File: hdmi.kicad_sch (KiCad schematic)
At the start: 58 parts, among them J13 HDMI-Mini-C_WE_685119136923, Q1 PJE138K, Q12 PJE138K, Q2 PJE138K, Q3 PJE138K, U36 TS3DV642RUARQ1, U43 NTS0102_XSON, U44 TPD4E05U06QDQARQ1, U45 TPD4E05U06QDQARQ1, U46 TPD4E05U06QDQARQ1

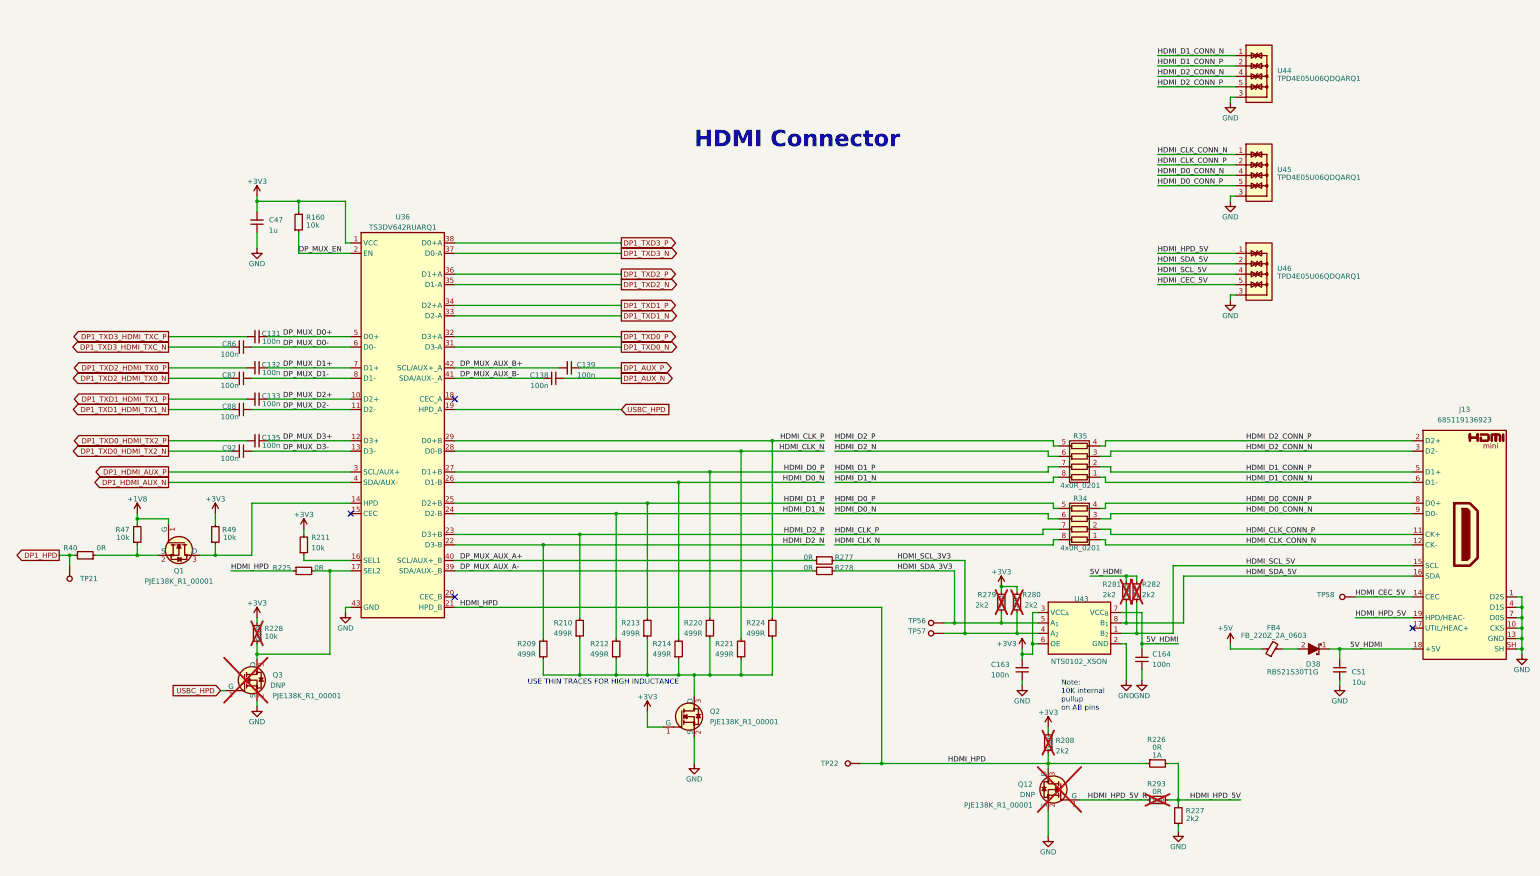
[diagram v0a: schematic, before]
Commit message: Schematic complete. Partial routing
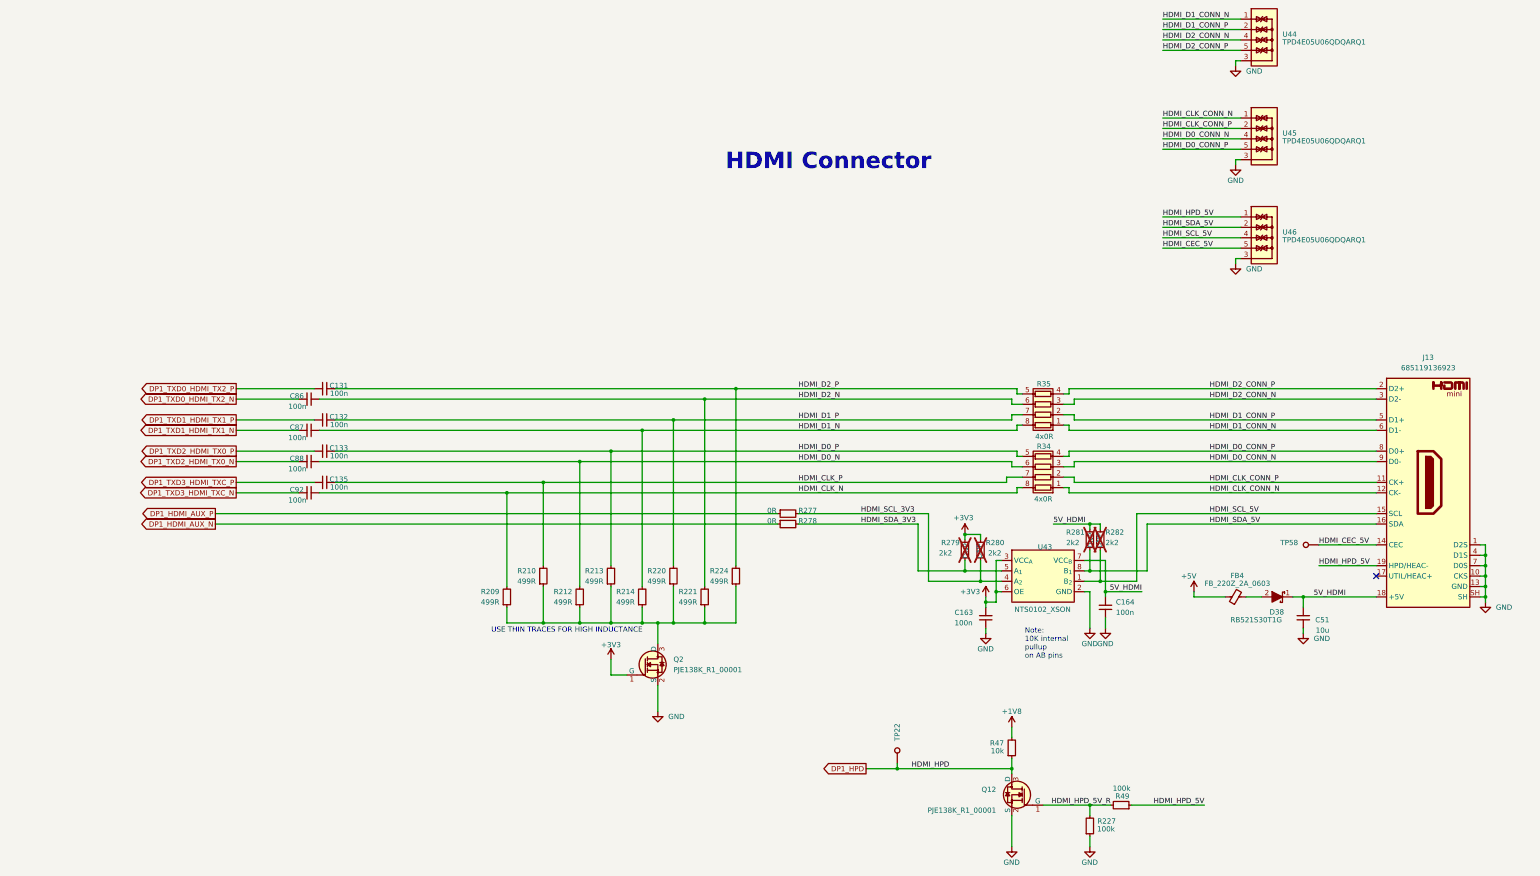
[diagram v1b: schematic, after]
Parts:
- removed C138, C139: C_100n_0402, antmicro-footprints:C_0402_1005Metric, symbol antmicroCapacitors0402:C_100n_0402
- removed C47: C_1u_0402, antmicro-footprints:C_0402_1005Metric, symbol antmicroCapacitors0402:C_1u_0402
- removed Q1, Q3: PJE138K, antmicro-footprints:SOT-523, symbol antmicroTransistorsFETsMOSFETsSingle:PJE138K
- removed R160, R211, R228, R49: R_10k_0402, antmicro-footprints:R_0402_1005Metric, symbol antmicroResistors0402:R_10k_0402
- removed R208: R_2k2_0402, antmicro-footprints:R_0402_1005Metric, symbol antmicroResistors0402:R_2k2_0402
- removed R225, R226, R293, R40: R_0R_0402, antmicro-footprints:R_0402_1005Metric, symbol antmicroResistors0402:R_0R_0402
- removed TP21, TP56, TP57: TP_0.75mm_SMD, antmicro-footprints:TP_SMD_0.75mm, symbol antmicroTestPoints:TP_0.75mm_SMD
- removed U36: TS3DV642RUARQ1, antmicro-footprints:WQFN-42-1EP_3.5x9mm_P0.5mm, symbol antmicroInterfaceAnalogSwitchesSpecialPurpose:TS3DV642RUARQ1
- added R49: R_100k_0603, Resistor_SMD:R_0603_1608Metric, symbol antmicroResistors0402:R_2k2_0402
- C131, C132, C133, C135, C86, C87, C88, C92: footprint antmicro-footprints:C_0402_1005Metric -> Capacitor_SMD:C_0402_1005Metric
- C163, C164: value C_100n_0402 -> C_100n_0603; footprint antmicro-footprints:C_0402_1005Metric -> Capacitor_SMD:C_0603_1608Metric
- C51: footprint antmicro-footprints:C_0603_1608Metric -> Capacitor_SMD:C_0603_1608Metric
- D38: footprint antmicro-footprints:SOD-523 -> Diode_SMD:D_SOD-523
- FB4: footprint antmicro-footprints:FB_0805_2012Metric -> Inductor_SMD:L_0603_1608Metric
- J13: footprint antmicro-footprints:HDMI-Mini-C_Receptacle_WE_685119136923 -> JetsonCarrier:HDMI-Mini-C_Receptacle_WE_685119136923
- Q12: footprint antmicro-footprints:SOT-523 -> Package_TO_SOT_SMD:SOT-523; now fitted
- Q2: footprint antmicro-footprints:SOT-523 -> Package_TO_SOT_SMD:SOT-523
- R209, R210, R212, R213, R214, R220, R221, R224, R277, R278, R279, R280, R281, R282: footprint antmicro-footprints:R_0402_1005Metric -> Resistor_SMD:R_0402_1005Metric
- R227: value R_2k2_0402 -> R_100k_0603; footprint antmicro-footprints:R_0402_1005Metric -> Resistor_SMD:R_0603_1608Metric; Val 2k2 -> 100k
- R34, R35: value R_4x0R_0201_array -> R_4x0R_0402_array; footprint antmicro-footprints:R_Array_4x0201_Panasonic_EXB18V -> Resistor_SMD:R_Array_Concave_4x0402; Val 4x0R_0201 -> 4x0R
- R47: value R_10k_0402 -> R_10k_0603; footprint antmicro-footprints:R_0402_1005Metric -> Resistor_SMD:R_0603_1608Metric
- TP22, TP58: footprint antmicro-footprints:TP_SMD_0.75mm -> JetsonCarrier:TP_SMD_0.75mm
- U43: footprint antmicro-footprints:XSON-8_1x1.95mm_P0.5mm -> JetsonCarrier:XSON-8_1x1.95mm_P0.5mm
- U44, U45, U46: footprint antmicro-footprints:USON-10_2.5x1mm_P0.5mm -> JetsonCarrier:USON-10_2.5x1mm_P0.5mm
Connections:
- net DP_MUX_AUX_A+ is gone; now on net DP1_HDMI_AUX_P: R277.1
- net DP_MUX_AUX_A- is gone; now on net DP1_HDMI_AUX_N: R278.1
- net DP_MUX_D0+ is gone; now on net HDMI_D2_P: C131.1
- net DP_MUX_D0- is gone; now on net HDMI_D2_N: C86.1
- net DP_MUX_D1+ is gone; now on net HDMI_D1_P: C132.1
- net DP_MUX_D1- is gone; now on net HDMI_D1_N: C87.1
- net DP_MUX_D2+ is gone; now on net HDMI_D0_P: C133.1
- net DP_MUX_D2- is gone; now on net HDMI_D0_N: C88.1
- net DP_MUX_D3+ is gone; now on net HDMI_CLK_P: C135.1
- net DP_MUX_D3- is gone; now on net HDMI_CLK_N: C92.1
- net HDMI_HPD is gone; now on net DP1_HPD: Q12.3 (D), TP22.1
- net DP1_HPD: now also R47.1
- net DP1_TXD0_HDMI_TX2_N: now also C86.2; no longer C92.2
- net DP1_TXD0_HDMI_TX2_P: now also C131.2; no longer C135.2
- net DP1_TXD1_HDMI_TX1_N: now also C87.2; no longer C88.2
- net DP1_TXD1_HDMI_TX1_P: now also C132.2; no longer C133.2
- net DP1_TXD2_HDMI_TX0_N: now also C88.2; no longer C87.2
- net DP1_TXD2_HDMI_TX0_P: now also C133.2; no longer C132.2
- net DP1_TXD3_HDMI_TXC_N: now also C92.2; no longer C86.2
- net DP1_TXD3_HDMI_TXC_P: now also C135.2; no longer C131.2
- net HDMI_CLK_N: now also R209.2; no longer R221.2
- net HDMI_CLK_P: now also R210.2; no longer R224.2
- net HDMI_D0_N: now also R212.2; no longer R214.2
- net HDMI_D0_P: now also R213.2; no longer R220.2
- net HDMI_D1_N: now also R214.2; no longer R212.2
- net HDMI_D1_P: now also R220.2; no longer R213.2
- net HDMI_D2_N: now also R221.2; no longer R209.2
- net HDMI_D2_P: now also R224.2; no longer R210.2
- net HDMI_HPD_5V: now also R49.1; no longer R227.2
- net HDMI_HPD_5V_R: now also R227.2, R49.2
- no-connect marks 4 -> 1
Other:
- company: Antmicro Ltd -> Argus-1 Cubesat
- title: Jetson Orin Baseboard -> Jetson Carrier Board
- moved on the sheet: C131, C132, C133, C135, C163, C164, C51, C86, C87, C88, C92, D38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
